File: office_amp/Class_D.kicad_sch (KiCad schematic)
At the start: 51 parts, among them J7 Screw_Terminal_01x04, Q6 BC856, Q7 BC850, Q8 BC856, Q9 BC856, U10 DS1882E, U12 TL082, U6 TPA3123D2

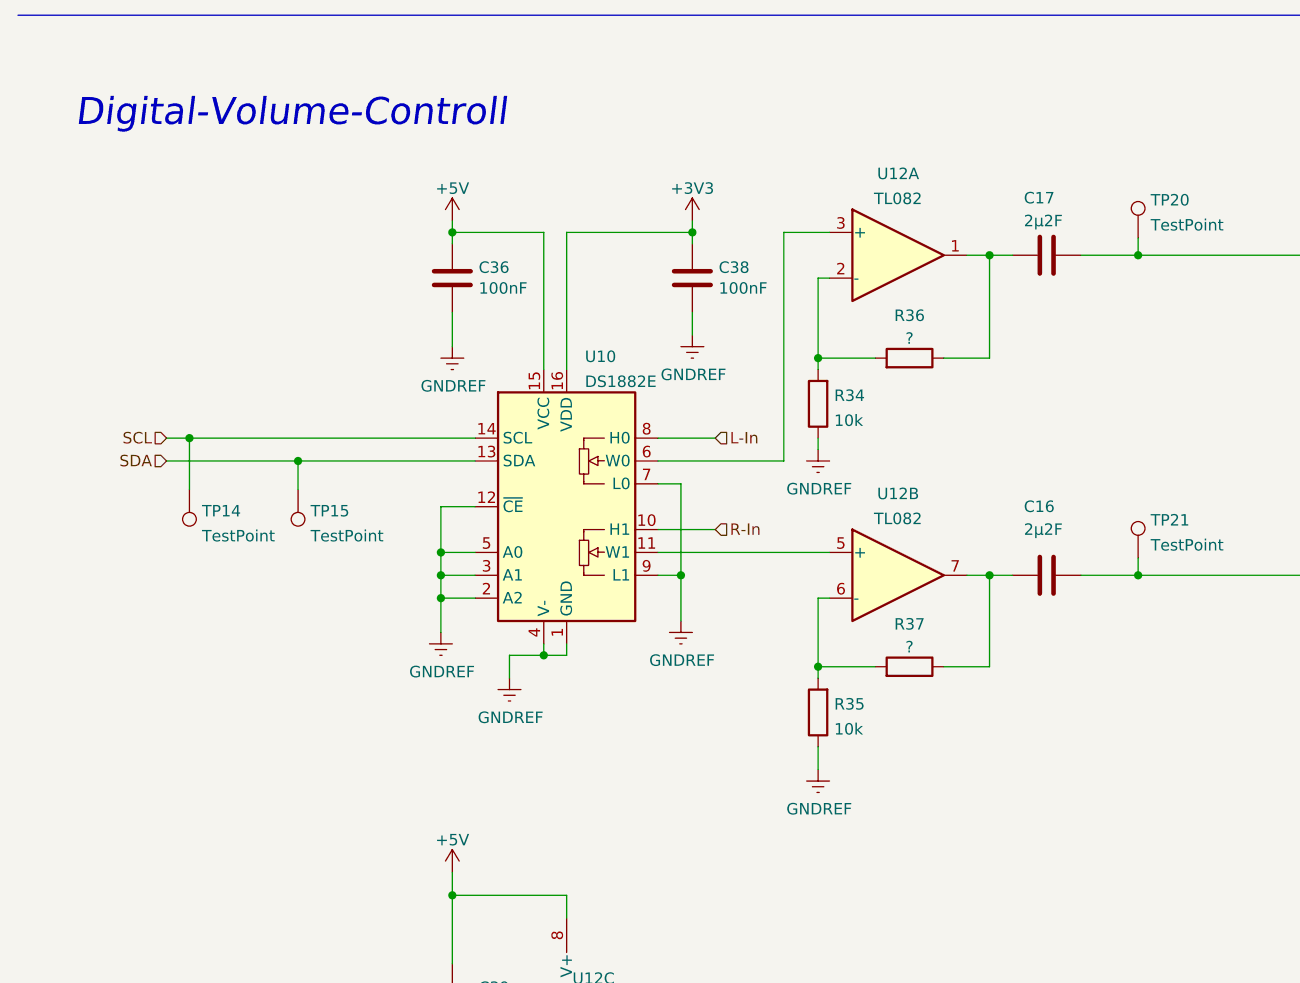
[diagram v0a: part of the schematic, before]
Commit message: error correction aftertest; corrected pinout touch; added level shifter for i2c poti; corrected voltages i2c poti
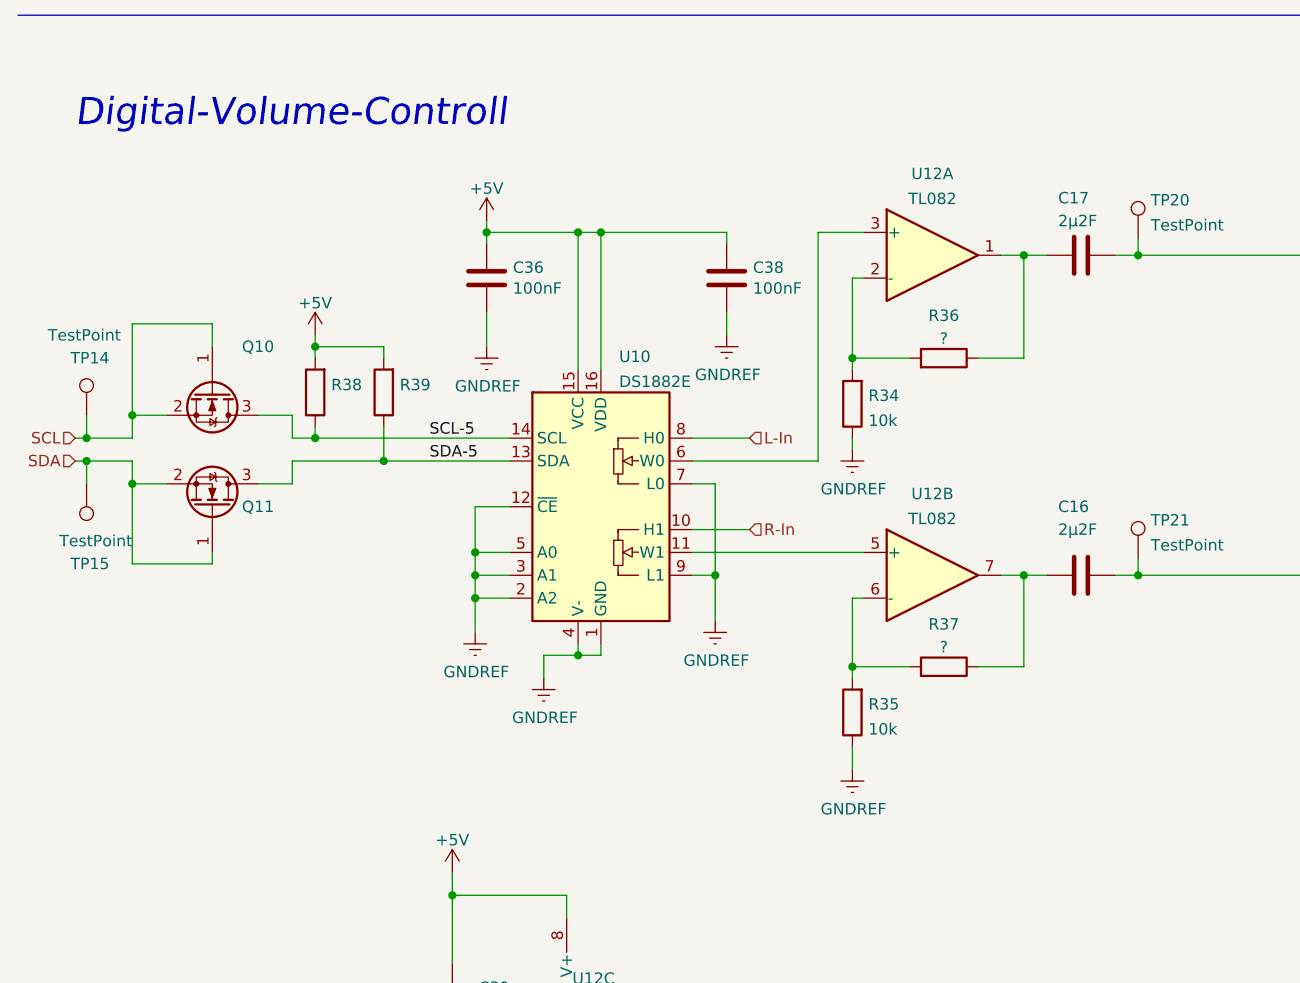
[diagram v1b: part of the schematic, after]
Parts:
- added Q10, Q11: (no value), symbol Transistor_FET:BSS138
- added R38, R39: (no value), symbol Device:R
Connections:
- net +3V3: no longer C38.1, U10.16 (VDD)
- net +5V: now also C38.1, U10.16 (VDD), R38.2, R39.2
- net SCL: now also Q10.1 (G), Q10.2 (S); no longer U10.14 (SCL)
- net SDA: now also Q11.1 (G), Q11.2 (S); no longer U10.13 (SDA)
- new net SCL-5: Q10.3 (D), R38.1, U10.14 (SCL)
- new net SDA-5: Q11.3 (D), R39.1, U10.13 (SDA)
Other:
- moved on the sheet: C16, C17, C36, C38, R34, R35, R36, R37, TP14, TP15, U10, U12A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

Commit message: new test software
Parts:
- Q10, Q11: value (none) -> BSS138; footprint (none) -> Package_TO_SOT_SMD:SOT-23
- R38, R39: value (none) -> 10k; footprint (none) -> Resistor_SMD:R_0805_2012Metric_Pad1.20x1.40mm_HandSolder
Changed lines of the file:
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@@
       (effects (font (size 1.27 1.27)) (justify right))
     )
-    (property "Value" "" (id 1) (at 47.498 183.3122 0)
-      (effects (font (size 1.27 1.27)) (justify right))
-    )
-    (property "Footprint" "" (id 2) (at 47.498 181.61 90)
+    (property "Value" "10k" (id 1) (at 47.498 183.3122 0)
+      (effects (font (size 1.27 1.27)) (justify right))
+    )
+    (property "Footprint" "Resistor_SMD:R_0805_2012Metric_Pad1.20x1.40mm_HandSolder" (id 2) (at 47.498 181.61 90)
       (effects (font (size 1.27 1.27)) hide)
     )
@@
       (effects (font (size 1.27 1.27)) (justify right))
     )
-    (property "Value" "" (id 1) (at 55.118 183.3122 0)
-      (effects (font (size 1.27 1.27)) (justify right))
-    )
-    (property "Footprint" "" (id 2) (at 55.118 181.61 90)
+    (property "Value" "10k" (id 1) (at 55.118 183.3122 0)
+      (effects (font (size 1.27 1.27)) (justify right))
+    )
+    (property "Footprint" "Resistor_SMD:R_0805_2012Metric_Pad1.20x1.40mm_HandSolder" (id 2) (at 55.118 181.61 90)
       (effects (font (size 1.27 1.27)) hide)
     )
@@
     (in_bom yes) (on_board yes)
     (property "Reference" "Q10" (id 0) (at 39.37 176.53 90))
-    (property "Value" "" (id 1) (at 39.37 179.0669 90))
-    (property "Footprint" "" (id 2) (at 32.385 186.69 0)
+    (property "Value" "BSS138" (id 1) (at 39.37 179.0669 90))
+    (property "Footprint" "Package_TO_SOT_SMD:SOT-23" (id 2) (at 32.385 186.69 0)
       (effects (font (size 1.27 1.27) italic) (justify left) hide)
     )
@@
     (in_bom yes) (on_board yes)
     (property "Reference" "Q11" (id 0) (at 39.37 194.3131 90))
-    (property "Value" "" (id 1) (at 39.37 196.85 90))
-    (property "Footprint" "" (id 2) (at 32.385 189.23 0)
+    (property "Value" "BSS138" (id 1) (at 39.37 196.85 90))
+    (property "Footprint" "Package_TO_SOT_SMD:SOT-23" (id 2) (at 32.385 189.23 0)
       (effects (font (size 1.27 1.27) italic) (justify left) hide)
     )

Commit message: changes from tim and josef, prototype
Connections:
- net +3V3: now also Q10.1 (G), Q11.1 (G)
- net GNDREF: no longer C39.2, U10.4 (V-), U12.4 (V-)
- net SCL: no longer Q10.1 (G)
- net SDA: no longer Q11.1 (G)
- new net -5V: C39.2, U10.4 (V-), U12.4 (V-)
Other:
- moved on the sheet: Q10

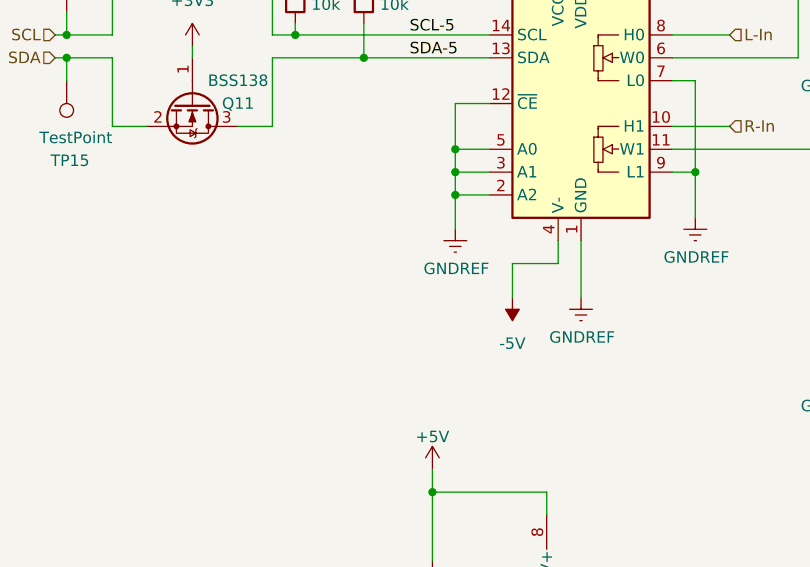
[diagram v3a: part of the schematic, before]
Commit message: Layout Amp done
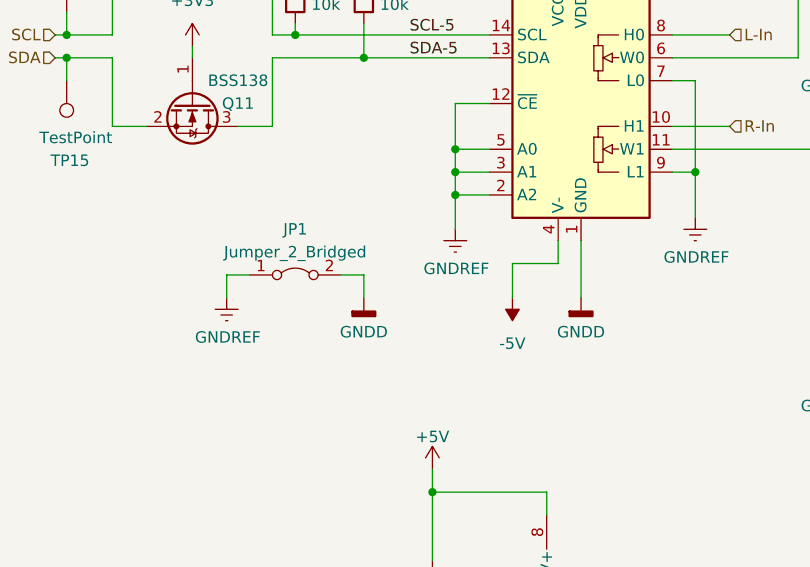
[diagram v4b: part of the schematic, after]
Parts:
- added JP1: Jumper_2_Bridged, Jumper:SolderJumper-2_P1.3mm_Bridged_Pad1.0x1.5mm, symbol Jumper:Jumper_2_Bridged
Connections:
- net GNDREF: now also JP1.1 (A); no longer U10.1 (GND)
- new net GNDD: JP1.2 (B), U10.1 (GND)
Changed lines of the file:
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@@
     (stroke (width 0) (type default))
   )
+  (wire (pts (xy 53.34 215.9) (xy 53.34 213.36))
+    (stroke (width 0) (type default))
+  )
   (wire (pts (xy 294.64 72.39) (xy 298.45 72.39))
     (stroke (width 0) (type default))
@@
     (stroke (width 0) (type default))
   )
+  (wire (pts (xy 38.1 213.36) (xy 38.1 215.9))
+    (stroke (width 0) (type default))
+  )
   (wire (pts (xy 119.38 212.09) (xy 124.46 212.09))
     (stroke (width 0) (type default))
@@
     (stroke (width 0) (type default))
   )
+  (wire (pts (xy 53.34 213.36) (xy 50.8 213.36))
+    (stroke (width 0) (type default))
+  )
   (wire (pts (xy 87.63 201.93) (xy 90.17 201.93))
     (stroke (width 0) (type default))
@@
     (stroke (width 0) (type default))
   )
+  (wire (pts (xy 40.64 213.36) (xy 38.1 213.36))
+    (stroke (width 0) (type default))
+  )
   (wire (pts (xy 76.2 88.9) (xy 76.2 90.17))
     (stroke (width 0) (type default))
@@
     )
   )
+  (symbol (lib_id "power:GNDREF") (at 38.1 215.9 0) (unit 1)
+    (in_bom yes) (on_board yes) (dnp no)
+    (property "Reference" "#PWR05" (at 38.1 222.25 0)
+      (effects (font (size 1.27 1.27)) hide)
+    )
+    (property "Value" "GNDREF" (at 38.227 220.2942 0)
+      (effects (font (size 1.27 1.27)))
+    )
+    (property "Footprint" "" (at 38.1 215.9 0)
+      (effects (font (size 1.27 1.27)) hide)
+    )
+    (property "Datasheet" "" (at 38.1 215.9 0)
+      (effects (font (size 1.27 1.27)) hide)
+    )
+    (pin "1")
+    (instances
+      (project "office_amp"
+        (path "/2de1ffee-2174-41d2-8969-68b8d21e5a7d/00000000-0000-0000-0000-0000602bbdaa"
+          (reference "#PWR05") (unit 1)
+        )
+      )
+    )
+  )
+  (symbol (lib_id "Jumper:Jumper_2_Bridged") (at 45.72 213.36 0) (unit 1)
+    (in_bom yes) (on_board yes) (dnp no) (fields_autoplaced)
+    (property "Reference" "JP1" (at 45.72 208.28 0)
+      (effects (font (size 1.27 1.27)))
+    )
+    (property "Value" "Jumper_2_Bridged" (at 45.72 210.82 0)
+      (effects (font (size 1.27 1.27)))
+    )
+    (property "Footprint" "Jumper:SolderJumper-2_P1.3mm_Bridged_Pad1.0x1.5mm" (at 45.72 213.36 0)
+      (effects (font (size 1.27 1.27)) hide)
+    )
+    (property "Datasheet" "~" (at 45.72 213.36 0)
+      (effects (font (size 1.27 1.27)) hide)
+    )
+    (pin "1")
+    (pin "2")
+    (instances
+      (project "office_amp"
+        (path "/2de1ffee-2174-41d2-8969-68b8d21e5a7d/00000000-0000-0000-0000-0000602bbdaa"
+          (reference "JP1") (unit 1)
+        )
+      )
+    )
+  )
   (symbol (lib_id "Device:R") (at 115.57 212.09 270) (mirror x) (unit 1)
     (in_bom yes) (on_board yes) (dnp no) (fields_autoplaced)
@@
     )
   )
+  (symbol (lib_id "power:GNDD") (at 53.34 215.9 0) (unit 1)
+    (in_bom yes) (on_board yes) (dnp no) (fields_autoplaced)
+    (property "Reference" "#PWR08" (at 53.34 222.25 0)
+      (effects (font (size 1.27 1.27)) hide)
+    )
+    (property "Value" "GNDD" (at 53.34 219.71 0)
+      (effects (font (size 1.27 1.27)))
+    )
+    (property "Footprint" "" (at 53.34 215.9 0)
+      (effects (font (size 1.27 1.27)) hide)
+    )
+    (property "Datasheet" "" (at 53.34 215.9 0)
+      (effects (font (size 1.27 1.27)) hide)
+    )
+    (pin "1")
+    (instances
+      (project "office_amp"
+        (path "/2de1ffee-2174-41d2-8969-68b8d21e5a7d/00000000-0000-0000-0000-0000602bbdaa"
+          (reference "#PWR08") (unit 1)
+        )
+      )
+    )
+  )
   (symbol (lib_id "power:GNDREF") (at 76.2 109.22 0) (unit 1)
     (in_bom yes) (on_board yes) (dnp no)
@@
     )
   )
+  (symbol (lib_id "power:GNDD") (at 77.47 215.9 0) (unit 1)
+    (in_bom yes) (on_board yes) (dnp no) (fields_autoplaced)
+    (property "Reference" "#PWR04" (at 77.47 222.25 0)
+      (effects (font (size 1.27 1.27)) hide)
+    )
+    (property "Value" "GNDD" (at 77.47 219.71 0)
+      (effects (font (size 1.27 1.27)))
+    )
+    (property "Footprint" "" (at 77.47 215.9 0)
+      (effects (font (size 1.27 1.27)) hide)
+    )
+    (property "Datasheet" "" (at 77.47 215.9 0)
+      (effects (font (size 1.27 1.27)) hide)
+    )
+    (pin "1")
+    (instances
+      (project "office_amp"
+        (path "/2de1ffee-2174-41d2-8969-68b8d21e5a7d/00000000-0000-0000-0000-0000602bbdaa"
+          (reference "#PWR04") (unit 1)
+        )
+      )
+    )
+  )
   (symbol (lib_id "power:GNDREF") (at 91.44 175.26 0) (unit 1)
     (in_bom yes) (on_board yes) (dnp no)
@@
         )
       )
-    )
-  )
-  (symbol (lib_name "GNDREF_1") (lib_id "power:GNDREF") (at 77.47 215.9 0) (unit 1)
-    (in_bom yes) (on_board yes) (dnp no)
-    (property "Reference" "#PWR049" (at 77.47 222.25 0)
-      (effects (font (size 1.27 1.27)) hide)
-    )
-    (property "Value" "GNDREF" (at 77.597 220.2942 0)
-      (effects (font (size 1.27 1.27)))
-    )
-    (property "Footprint" "" (at 77.47 215.9 0)
-      (effects (font (size 1.27 1.27)) hide)
-    )
-    (property "Datasheet" "" (at 77.47 215.9 0)
-      (effects (font (size 1.27 1.27)) hide)
-    )
-    (pin "1")
-    (instances
-      (project "office_amp"
-        (path "/2de1ffee-2174-41d2-8969-68b8d21e5a7d/00000000-0000-0000-0000-0000602bbdaa"
-          (reference "#PWR049") (unit 1)
-        )
-      )
